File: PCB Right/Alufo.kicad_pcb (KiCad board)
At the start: 2 copper layers, 282.6 x 90.9 mm, 94 parts, among them J2 USB_C_Receptacle_USB2.0_16P_2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, J4 USB_C_Receptacle_USB2.0_16P_2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, K11 PG1350, K12 PG1350, K13 PG1350, K14 PG1350, K15 PG1350, K16 PG1350, K21 PG1350, K22 PG1350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

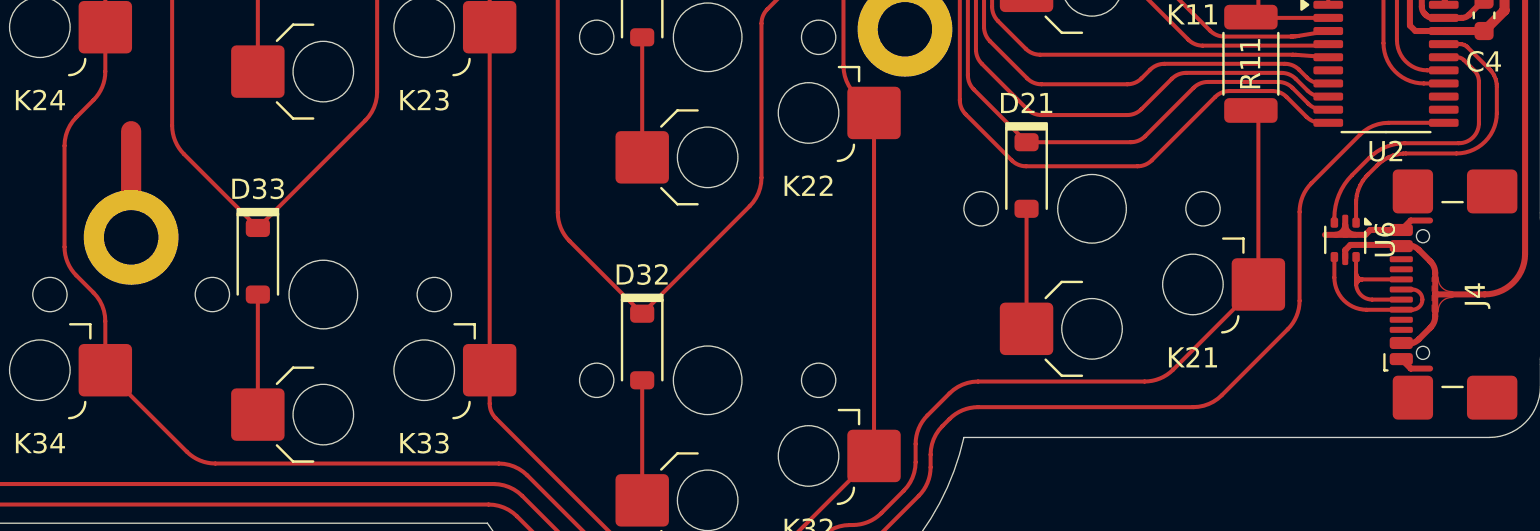
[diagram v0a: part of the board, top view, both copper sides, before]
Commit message: Add ferrite bead to righthand side split connector port
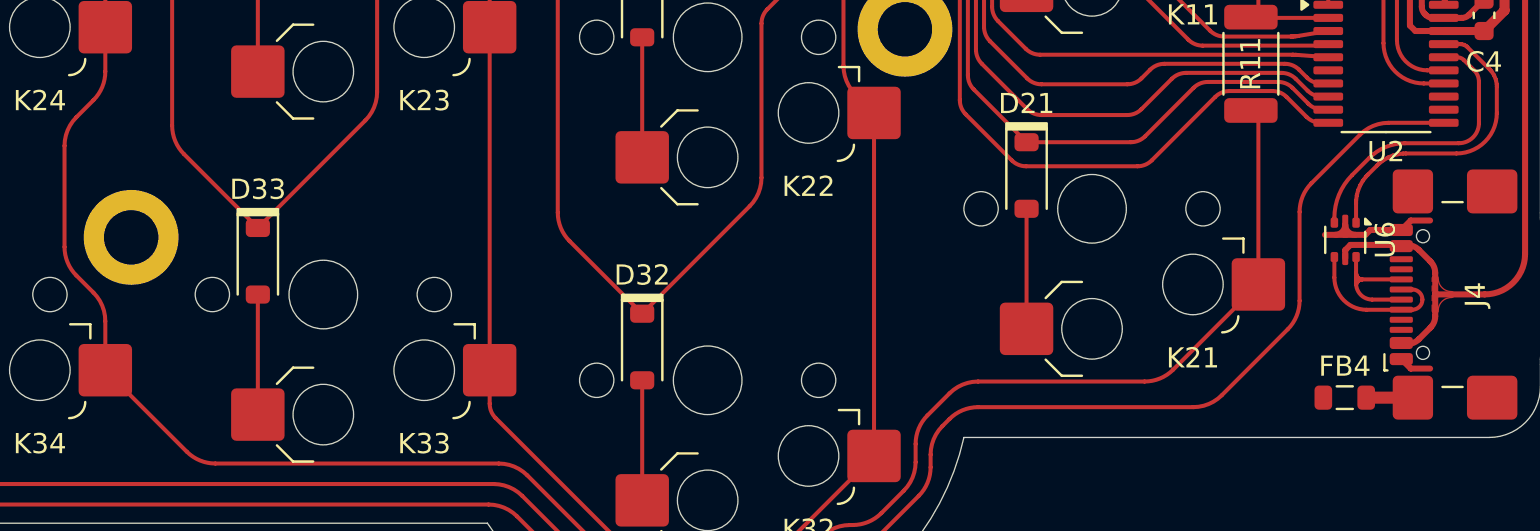
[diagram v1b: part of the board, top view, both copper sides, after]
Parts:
- added FB4: FerriteBead, Inductor_SMD:L_0805_2012Metric, F.Cu at (155.4, 78.8)
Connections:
- J4 pad S2: unconnected-(J4-SHIELD-PadS2) -> Net-(FB4-Pad1)
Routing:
- net (no net): track 5.27 -> 0.00 mm
- net Net-(FB4-Pad1): track 0.00 -> 2.31 mm
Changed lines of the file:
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@@
 	(net 30 "unconnected-(J4-SBU2-PadB8)")
 	(net 31 "unconnected-(J4-CC2-PadB5)")
-	(net 32 "unconnected-(J4-SHIELD-PadS2)")
+	(net 32 "unconnected-(FB4-Pad2)")
 	(net 33 "unconnected-(J4-SHIELD-PadS4)")
 	(net 34 "unconnected-(J4-SHIELD-PadS3)")
@@
 	(net 71 "USB+")
 	(net 72 "USB-")
+	(net 73 "Net-(FB4-Pad1)")
 	(footprint "Project_Library:SW_choc_v1_HS_CPG135001S30_1layer_1u"
 		(layer "F.Cu")
@@
 		(embedded_fonts no)
 	)
+	(footprint "Inductor_SMD:L_0805_2012Metric"
+		(layer "F.Cu")
+		(at 155.4015 78.776684 180)
+		(descr "Inductor SMD 0805 (2012 Metric), square (rectangular) end terminal, IPC-7351 nominal, (Body size source: IPC-SM-782 page 80, https://www.pcb-3d.com/wordpress/wp-content/uploads/ipc-sm-782a_amendment_1_and_2.pdf), generated with kicad-footprint-generator")
+		(tags "inductor")
+		(property "Reference" "FB4"
+			(at 0 1.550001 0)
+			(layer "F.SilkS")
+			(effects
+				(font
+					(size 1 1)
+					(thickness 0.15)
+				)
+			)
+		)
+		(property "Value" "FerriteBead"
+			(at 0 1.550001 0)
+			(layer "F.Fab")
+			(effects
+				(font
+					(size 1 1)
+					(thickness 0.15)
+				)
+			)
+		)
+		(property "Datasheet" ""
+			(at 0 0 0)
+			(layer "F.Fab")
+			(hide yes)
+			(effects
+				(font
+					(size 1.27 1.27)
+					(thickness 0.15)
+				)
+			)
+		)
+		(property "Description" "Ferrite bead"
+			(at 0 0 0)
+			(layer "F.Fab")
+			(hide yes)
+			(effects
+				(font
+					(size 1.27 1.27)
+					(thickness 0.15)
+				)
+			)
+		)
+		(property "LCSC" "C20416196"
+			(at 0 0 180)
+			(unlocked yes)
+			(layer "F.Fab")
+			(hide yes)
+			(effects
+				(font
+					(size 1 1)
+					(thickness 0.15)
+				)
+			)
+		)
+		(property ki_fp_filters "Inductor_* L_* *Ferrite*")
+		(sheetname "/")
+		(sheetfile "Alufo.kicad_sch")
+		(attr smd)
+		(fp_line
+			(start -0.399622 0.56)
+			(end 0.399622 0.56)
+			(stroke
+				(width 0.12)
+				(type solid)
+			)
+			(layer "F.SilkS")
+		)
+		(fp_line
+			(start -0.399622 -0.56)
+			(end 0.399622 -0.56)
+			(stroke
+				(width 0.12)
+				(type solid)
+			)
+			(layer "F.SilkS")
+		)
+		(fp_line
+			(start 1.75 0.85)
+			(end -1.75 0.85)
+			(stroke
+				(width 0.05)
+				(type solid)
+			)
+			(layer "F.CrtYd")
+		)
+		(fp_line
+			(start 1.75 -0.85)
+			(end 1.75 0.85)
+			(stroke
+				(width 0.05)
+				(type solid)
+			)
+			(layer "F.CrtYd")
+		)
+		(fp_line
+			(start -1.75 0.85)
+			(end -1.75 -0.85)
+			(stroke
+				(width 0.05)
+				(type solid)
+			)
+			(layer "F.CrtYd")
+		)
+		(fp_line
+			(start -1.75 -0.85)
+			(end 1.75 -0.85)
+			(stroke
+				(width 0.05)
+				(type solid)
+			)
+			(layer "F.CrtYd")
+		)
+		(fp_line
+			(start 1 0.45)
+			(end -1 0.45)
+			(stroke
+				(width 0.1)
+				(type solid)
+			)
+			(layer "F.Fab")
+		)
+		(fp_line
+			(start 1 -0.45)
+			(end 1 0.45)
+			(stroke
+				(width 0.1)
+				(type solid)
+			)
+			(layer "F.Fab")
+		)
+		(fp_line
+			(start -1 0.45)
+			(end -1 -0.45)
+			(stroke
+				(width 0.1)
+				(type solid)
+			)
+			(layer "F.Fab")
+		)
+		(fp_line
+			(start -1 -0.45)
+			(end 1 -0.45)
+			(stroke
+				(width 0.1)
+				(type solid)
+			)
+			(layer "F.Fab")
+		)
+		(fp_text user "${REFERENCE}"
+			(at 0 0 0)
+			(layer "F.Fab")
+			(effects
+				(font
+					(size 0.5 0.5)
+					(thickness 0.08)
+				)
+			)
+		)
+		(pad "1" smd roundrect
+			(at -1.0625 0 180)
+			(size 0.875 1.2)
+			(layers "F.Cu" "F.Mask" "F.Paste")
+			(roundrect_rratio 0.25)
+			(net 73 "Net-(FB4-Pad1)")
+			(pintype "passive")
+		)
+		(pad "2" smd roundrect
+			(at 1.0625 0 180)
+			(size 0.875 1.2)
+			(layers "F.Cu" "F.Mask" "F.Paste")
+			(roundrect_rratio 0.25)
+			(net 32 "unconnected-(FB4-Pad2)")
+			(pintype "passive")
+		)
+		(embedded_fonts no)
+		(model "${KICAD9_3DMODEL_DIR}/Inductor_SMD.3dshapes/L_0805_2012Metric.wrl"
+			(offset
+				(xyz 0 0 0)
+			)
+			(scale
+				(xyz 1 1 1)
+			)
+			(rotate
+				(xyz 0 0 0)
+			)
+		)
+	)
 	(footprint "Project_Library:NetTie-2_SMD_Pad0.2mm"
 		(layer "F.Cu")
@@
 			(layers "F.Cu" "F.Mask" "F.Paste")
 			(roundrect_rratio 0.125)
-			(net 32 "unconnected-(J4-SHIELD-PadS2)")
+			(net 73 "Net-(FB4-Pad1)")
 			(pinfunction "SHIELD")
-			(pintype "passive+no_connect")
+			(pintype "passive")
 			(thermal_bridge_angle 45)
 		)
@@
 	)
 	(segment
-		(start 95.25 65.567997)
-		(end 95.25 70.83335)
-		(width 1)
-		(layer "F.Cu")
-		(net 0)
-	)
-	(segment
 		(start 63.43 83.866684)
 		(end 63.43 77.916684)
@@
 		(net 72)
 	)
+	(segment
+		(start 156.464 78.776684)
+		(end 158.778 78.776684)
+		(width 0.6)
+		(layer "F.Cu")
+		(net 73)
+	)
 	(zone

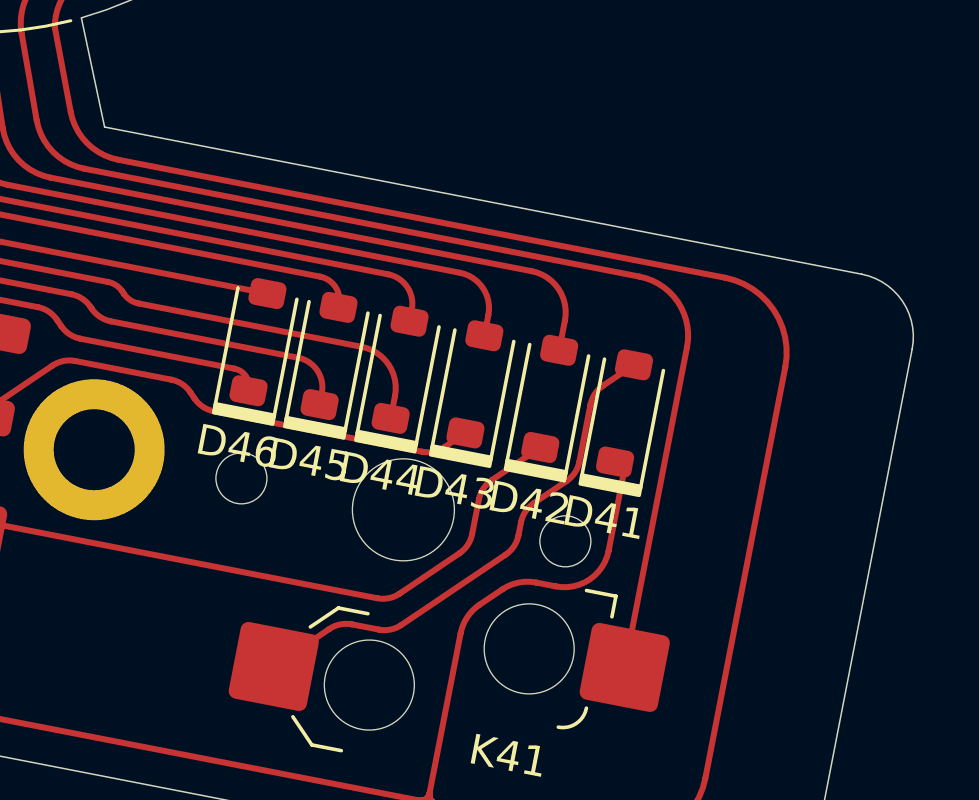
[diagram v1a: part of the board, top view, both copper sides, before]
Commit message: Add warning for nav. switch diode’s direction
Also fixed these diode’s labels, which had reset to a bad location.
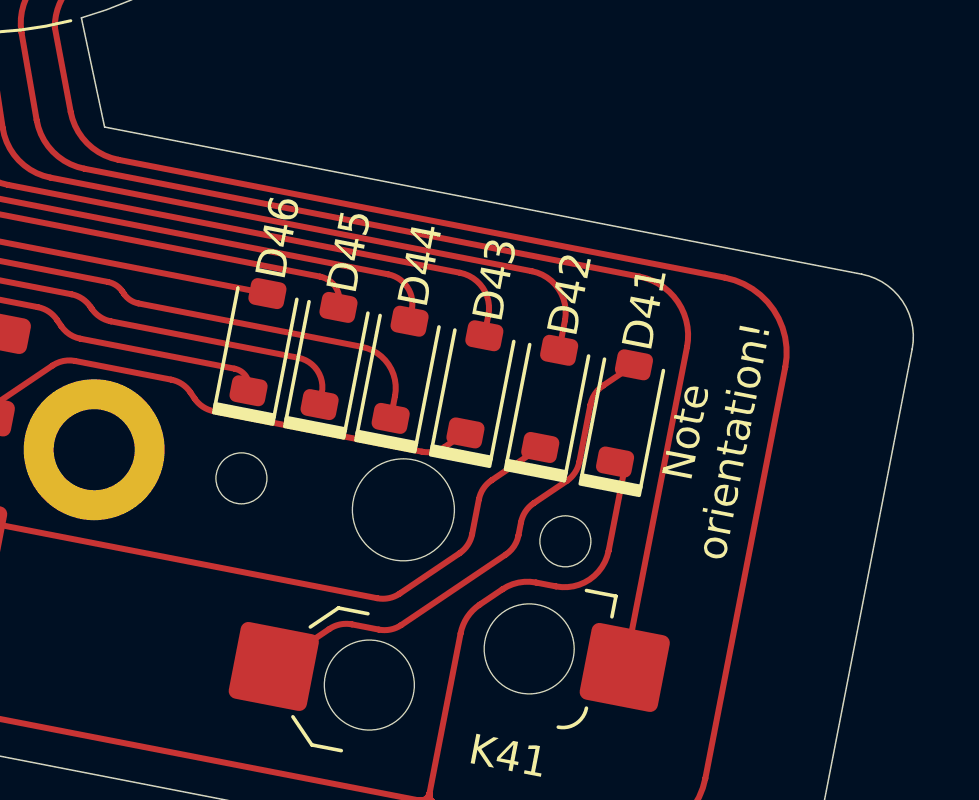
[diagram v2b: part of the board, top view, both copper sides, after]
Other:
- board text added: "Note orientation!"
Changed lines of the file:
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@@
 		(tags "SOD-123")
 		(property "Reference" "D45"
-			(at -3.556 0.000001 349)
+			(at 3.556 0.000001 79)
 			(layer "F.SilkS")
 			(effects
@@
 		(tags "SOD-123")
 		(property "Reference" "D43"
-			(at -3.556 0.000001 349)
+			(at 3.556 0.000001 79)
 			(layer "F.SilkS")
 			(effects
@@
 		(tags "SOD-123")
 		(property "Reference" "D44"
-			(at -3.556 0.000001 349)
+			(at 3.556 0.000001 79)
 			(layer "F.SilkS")
 			(effects
@@
 		(tags "SOD-123")
 		(property "Reference" "D46"
-			(at -3.556 0.000001 349)
+			(at 3.556 0.000001 79)
 			(layer "F.SilkS")
 			(effects
@@
 		(tags "SOD-123")
 		(property "Reference" "D42"
-			(at -3.556 0.000001 349)
+			(at 3.556 0.000001 79)
 			(layer "F.SilkS")
 			(effects
@@
 		(tags "SOD-123")
 		(property "Reference" "D41"
-			(at -3.556 0.000001 349)
+			(at 3.556 0.000001 79)
 			(layer "F.SilkS")
 			(effects
@@
 			)
 		)
+	)
+	(gr_text "Note\norientation!"
+		(at 148.336 104.394 79)
+		(layer "F.SilkS")
+		(effects
+			(font
+				(size 1 1)
+				(thickness 0.15)
+			)
+		)

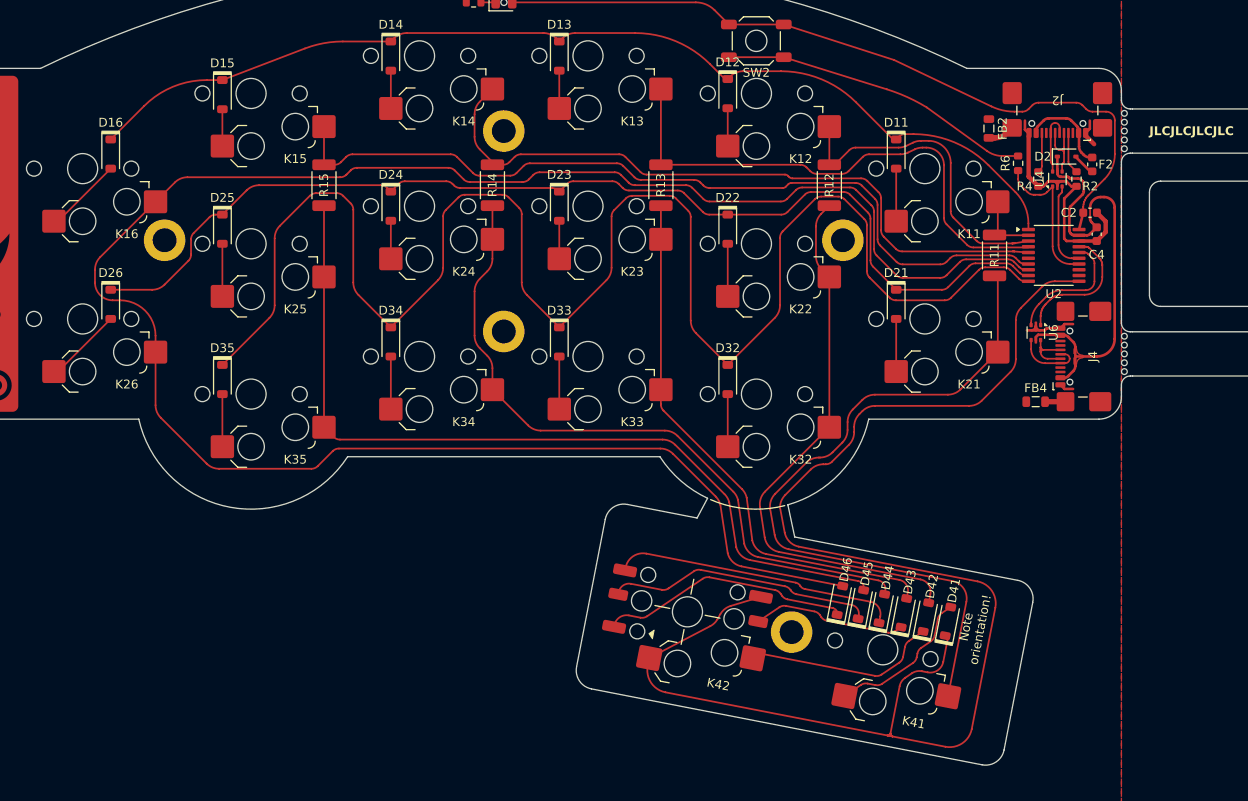
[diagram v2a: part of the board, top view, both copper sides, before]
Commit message: Proof-of-concept: One USB C port on right side
The right hand PCB has been setup to have a single USB C port that can handle either bootloader duties or split connection via the side band channels.
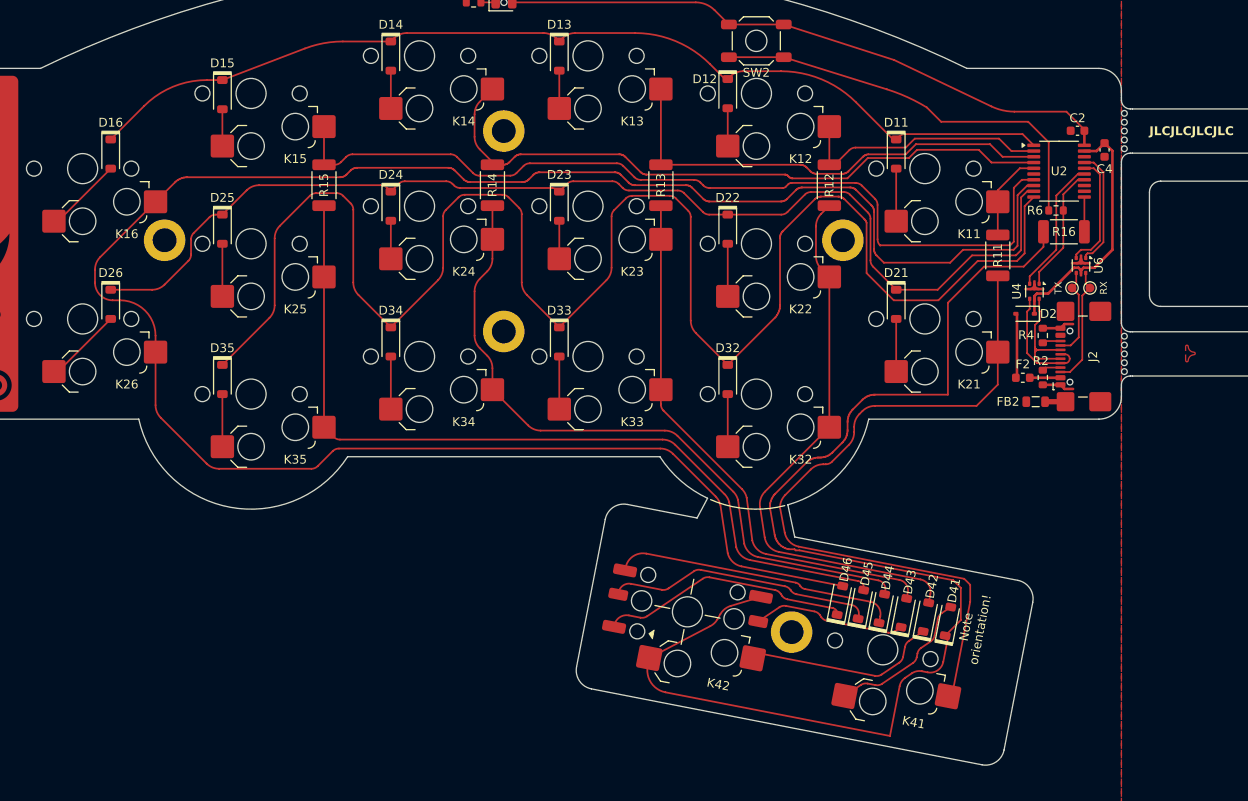
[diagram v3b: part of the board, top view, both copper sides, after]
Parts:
- removed FB4: FerriteBead, Inductor_SMD:L_0805_2012Metric
- removed the J2 at (157.9, 44.7)
- removed NT2: NetTie_2, Project_Library:NetTie-2_SMD_Pad0.2mm
- added R16: 0R, Resistor_SMD:R_2010_5025Metric, F.Cu at (158.6, 59.6)
- added TP2: RX, TestPoint:TestPoint_Pad_D1.0mm, F.Cu at (161.5, 65.9)
- added TP4: TX, TestPoint:TestPoint_Pad_D1.0mm, F.Cu at (159.5, 65.9)
- moved FB2 31.3 mm to (155.4, 78.8), turned to 180 degrees
- moved F2 25.4 mm to (153.9, 76.1), turned to 180 degrees
- moved R2 22.8 mm to (156.2, 76.0)
- moved D2 18.4 mm to (154.2, 68.8), turned to 180 degrees
- moved R4 17.7 mm to (156.2, 71.3), turned to 90 degrees
- moved U4 13.0 mm to (155.3, 66.3), turned to -90 degrees
- moved C4 9.57 mm to (163.2, 50.3)
- moved U2 9.54 mm to (158.0, 52.7)
- moved C2 9.38 mm to (160.1, 48.1), turned to 180 degrees
- moved U6 9.14 mm to (160.5, 63.4)
- moved R6 6.84 mm to (157.7, 57.1), turned to 180 degrees
- moved R11 0.37 mm to (151.1, 62.2)
- renumbered J4 to J2
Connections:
- D41 pad 1: Row4 -> Row4T
- J2 pad A4: VCC -> VBUS
- J2 pad A5: unconnected-(J4-CC1-PadA5) -> Net-(J2-CC1)
- J2 pad A6: RX_P -> USB_P+
- J2 pad A7: TX_P -> USB_P-
- J2 pad A8: unconnected-(J4-SBU1-PadA8) -> TX_P
- J2 pad A9: VCC -> VBUS
- J2 pad B4: VCC -> VBUS
- J2 pad B5: unconnected-(J4-CC2-PadB5) -> Net-(J2-CC2)
- J2 pad B6: RX_P -> USB_P+
- J2 pad B7: TX_P -> USB_P-
- J2 pad B8: unconnected-(J4-SBU2-PadB8) -> RX_P
- J2 pad B9: VCC -> VBUS
- J2 pad S2: Net-(FB4-Pad1) -> Net-(FB2-Pad1)
- K42 pad 4: Row4 -> Row4T
- R6 pad 1: Net-(NT2-Pad2) -> USB+
- U2 pad 2: Col1 -> Col2
- U2 pad 3: Col2 -> Col3
- U2 pad 4: Col3 -> Col4
- U2 pad 5: Col4 -> Col1
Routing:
- net Row4: track 162.0 -> 3.93 mm
- net Row4T: track 0.00 -> 143.8 mm
- net GND: track 34.0 -> 7.23 mm
- net VCC: track 52.0 -> 28.7 mm
- net +3V3: track 85.7 -> 70.0 mm
- net BOOT: track 35.4 -> 46.5 mm
- net USB_P-: track 5.48 -> 13.9 mm
- net RX_P: track 5.49 -> 13.4 mm
- net Row2: track 122.5 -> 129.9 mm
- net Col3: track 60.0 -> 53.0 mm
- net Col2: track 35.2 -> 28.2 mm
- net Row3: track 185.6 -> 192.6 mm
- net Col6: track 230.6 -> 236.7 mm
- net Col5: track 92.4 -> 98.5 mm
- net VBUS: track 9.41 -> 3.47 mm
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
